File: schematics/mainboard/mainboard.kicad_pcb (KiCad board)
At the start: 2 copper layers, 86.1 x 79.8 mm, 71 parts, among them J1 ICSP, J10 Conn_01x02_Pin, J2 USB_B_Micro, J3 DEALON DC-S050-200, J4 PWR_SELECT, J5 JOY1, J6 JOY2, J7 Conn_01x06_Pin, J8 DGAUGES, J9 LCD, Q2 BC849, U1 ATmega2560-16A, U2 FT232RL, U3 USBLC6-2P6, U4 AIP78M05, U5 L9110, U6 74HC595, U7 74HC595, U8 74HC165, Y1 16Mhz

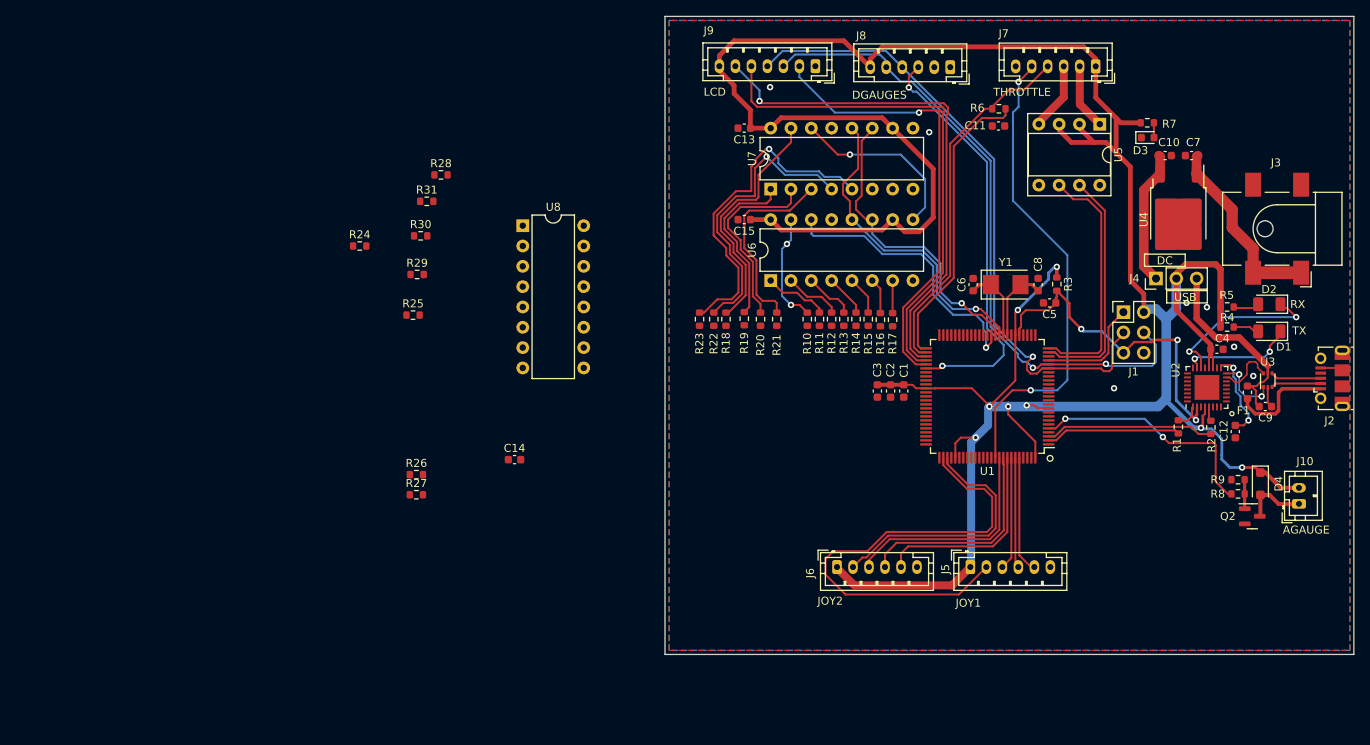
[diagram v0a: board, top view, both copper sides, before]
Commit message: SCH: Mainboard=> LED/Buttons routing(2)
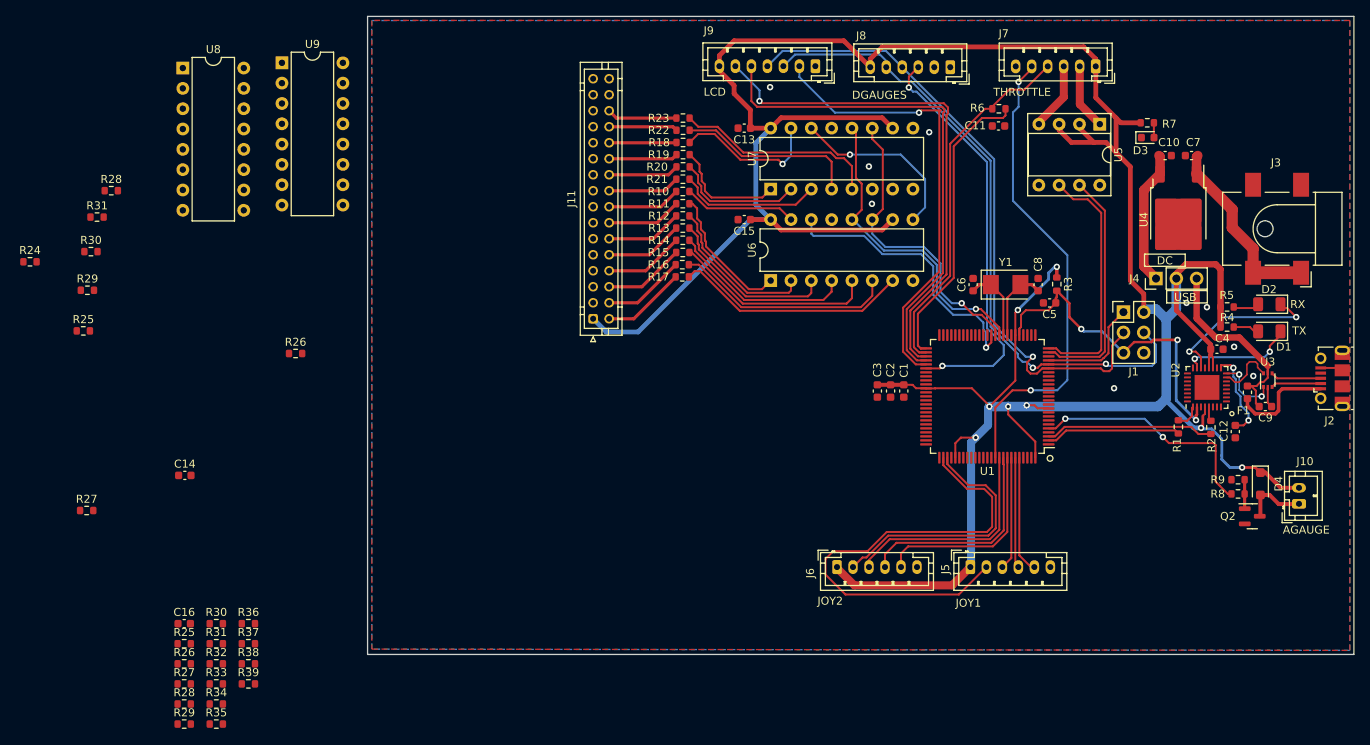
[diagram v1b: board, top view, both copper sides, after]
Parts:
- added C16: 0.1 µf, Capacitor_SMD:C_0603_1608Metric, F.Cu at (58.3, 98.3)
- added J11: Conn_02x16_Counter_Clockwise, Connector_JST:JST_PHD_B32B-PHDSS_2x16_P2.00mm_Vertical, F.Cu at (109.4, 60.1)
- added R25: 10K, Resistor_SMD:R_0603_1608Metric, F.Cu at (58.3, 100.8)
- added R26: 10K, Resistor_SMD:R_0603_1608Metric, F.Cu at (58.3, 103.3)
- added R27: 10K, Resistor_SMD:R_0603_1608Metric, F.Cu at (58.3, 105.8)
- added R28: 10K, Resistor_SMD:R_0603_1608Metric, F.Cu at (58.3, 108.3)
- added R29: 10K, Resistor_SMD:R_0603_1608Metric, F.Cu at (58.3, 110.8)
- added R30: 10K, Resistor_SMD:R_0603_1608Metric, F.Cu at (62.3, 98.3)
- added R31: 10K, Resistor_SMD:R_0603_1608Metric, F.Cu at (62.3, 100.8)
- added R32: 10K, Resistor_SMD:R_0603_1608Metric, F.Cu at (62.3, 103.3)
- added R33: 10K, Resistor_SMD:R_0603_1608Metric, F.Cu at (62.3, 105.8)
- added R34: 10K, Resistor_SMD:R_0603_1608Metric, F.Cu at (62.3, 108.3)
- added R35: 10K, Resistor_SMD:R_0603_1608Metric, F.Cu at (62.3, 110.8)
- added R36: 10K, Resistor_SMD:R_0603_1608Metric, F.Cu at (66.3, 98.3)
- added R37: 10K, Resistor_SMD:R_0603_1608Metric, F.Cu at (66.3, 100.8)
- added R38: 10K, Resistor_SMD:R_0603_1608Metric, F.Cu at (66.3, 103.3)
- added R39: 10K, Resistor_SMD:R_0603_1608Metric, F.Cu at (66.3, 105.8)
- added U9: 74HC165, Package_DIP:DIP-16_W7.62mm, F.Cu at (70.5, 28.2)
- R24: value R? -> 10K
- moved U8 46.8 mm to (58.1, 28.8)
- moved C14 41.3 mm to (58.3, 79.7)
- moved R27 41.3 mm to (46.1, 84.1)
- moved R28 41.3 mm to (49.1, 44.1)
- moved R29 41.3 mm to (46.2, 56.6)
- moved R30 41.3 mm to (46.6, 51.8)
- moved R31 41.3 mm to (47.4, 47.4)
- moved R24 41.3 mm to (39.0, 53.0)
- moved R25 41.3 mm to (45.7, 61.7)
- moved R17 26.8 mm to (120.5, 54.9), turned to 0 degrees
- moved R16 25.7 mm to (120.5, 53.4), turned to 0 degrees
- moved R23 25.2 mm to (120.6, 35.1), turned to 0 degrees
- moved R15 24.6 mm to (120.6, 51.9), turned to 0 degrees
- moved R22 23.9 mm to (120.6, 36.6), turned to 0 degrees
- moved R14 23.8 mm to (120.6, 50.3), turned to 0 degrees
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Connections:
- R10 pad 1: unconnected-(R10-Pad1) -> /QAU6
- R11 pad 1: unconnected-(R11-Pad1) -> /QBU6
- R12 pad 1: unconnected-(R12-Pad1) -> /QCU6
- R13 pad 1: unconnected-(R13-Pad1) -> /QDU6
- R14 pad 1: unconnected-(R14-Pad1) -> /QEU6
- R15 pad 1: unconnected-(R15-Pad1) -> /QFU6
- R16 pad 1: unconnected-(R16-Pad1) -> /QGU6
- R17 pad 1: unconnected-(R17-Pad1) -> /QHU6
- R18 pad 1: unconnected-(R18-Pad1) -> /QAU7
- R19 pad 1: unconnected-(R19-Pad1) -> /QBU7
- R20 pad 1: unconnected-(R20-Pad1) -> /QCU7
- R21 pad 1: unconnected-(R21-Pad1) -> /QDU7
- R22 pad 1: unconnected-(R22-Pad1) -> /QEU7
- R23 pad 1: unconnected-(R23-Pad1) -> /QFU7
- R24 pad 2: unconnected-(R24-Pad2) -> GND
- U7 pad 6: unconnected-(U7-QG-Pad6) -> GND
- U7 pad 7: unconnected-(U7-QH-Pad7) -> GND
- U7 pad 9: unconnected-(U7-QH'-Pad9) -> GND
- U8 pad 1: unconnected-(U8-~{PL}-Pad1) -> /LATCH
- U8 pad 15: unconnected-(U8-~{CE}-Pad15) -> GND
- U8 pad 2: unconnected-(U8-CP-Pad2) -> /SCK
- U8 pad 7: unconnected-(U8-~{Q7}-Pad7) -> GND
- U8 pad 9: unconnected-(U8-Q7-Pad9) -> Net-(U8-Q7)
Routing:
- net Net-(U6-QH): track 4.06 -> 29.4 mm
- net Net-(U6-QG): track 4.48 -> 27.6 mm
- net +5V: track 357.7 -> 379.6 mm
- net Net-(U6-QF): track 4.84 -> 25.5 mm
- net Net-(U6-QE): track 5.26 -> 23.0 mm
- net Net-(U7-QF): track 42.1 -> 25.7 mm, vias 1 -> 0
- net Net-(U6-QD): track 6.28 -> 21.4 mm
- net Net-(U7-QE): track 36.7 -> 22.8 mm, vias 1 -> 0
- net Net-(U6-QC): track 7.15 -> 19.4 mm
- net Net-(U7-QA): track 30.5 -> 18.5 mm, vias 0 -> 1
- net /QHU6: track 0.00 -> 10.5 mm
- net /QGU6: track 0.00 -> 10.3 mm
- net /QFU6: track 0.00 -> 10.2 mm
- net /QEU6: track 0.00 -> 9.96 mm
- net /QDU6: track 0.00 -> 9.76 mm
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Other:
- board size 86.1 x 79.8 mm -> 123.3 x 79.8 mm

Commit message: SCH: MAinboard=> Clean DRC issues
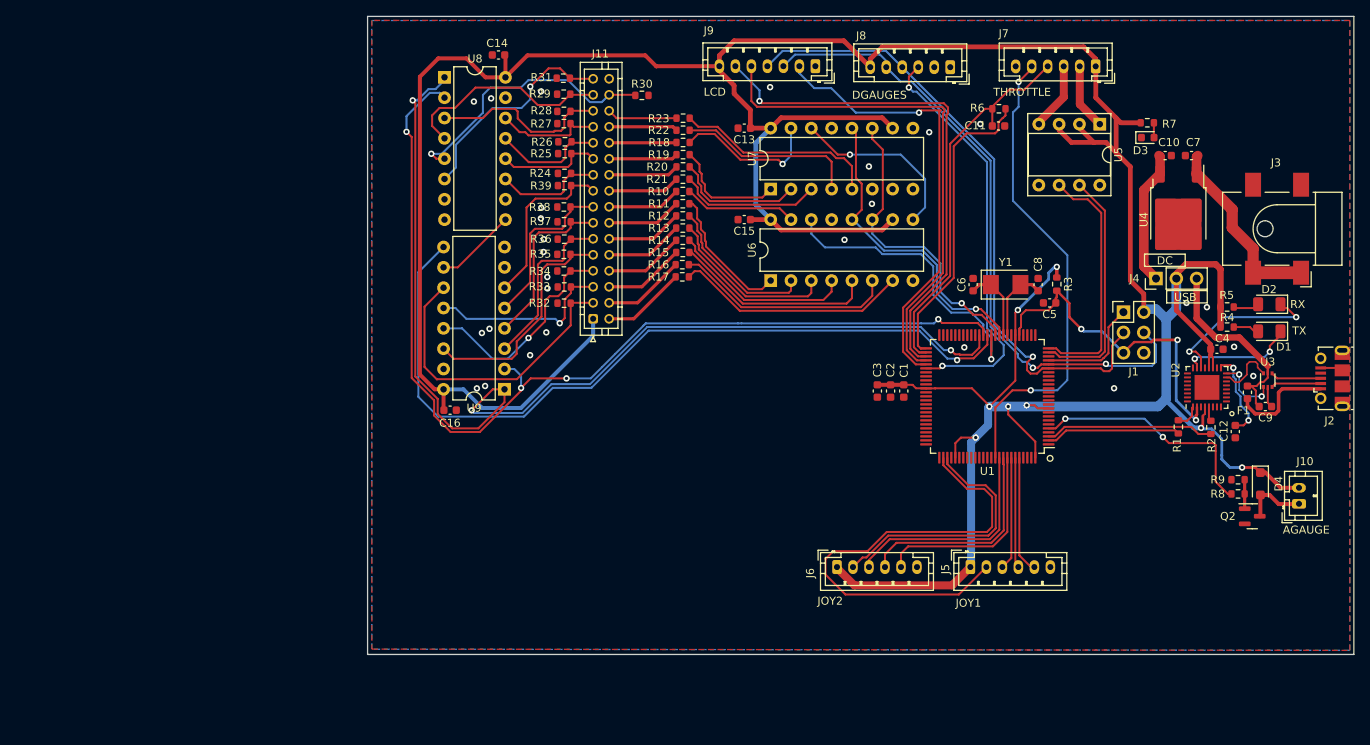
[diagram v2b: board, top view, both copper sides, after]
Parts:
- removed the R25 at (58.3, 100.8)
- removed the R25 at (45.7, 61.7)
- removed the R26 at (72.2, 64.5)
- removed the R26 at (58.3, 103.3)
- removed the R27 at (58.3, 105.8)
- removed the R27 at (46.1, 84.1)
- removed the R28 at (49.1, 44.1)
- removed the R28 at (58.3, 108.3)
- removed the R29 at (58.3, 110.8)
- removed the R29 at (46.2, 56.6)
- removed the R30 at (62.3, 98.3)
- removed the R30 at (46.6, 51.8)
- removed the R31 at (47.4, 47.4)
- removed the R31 at (62.3, 100.8)
- added R25: 10K, Resistor_SMD:R_0603_1608Metric, F.Cu at (105.8, 39.5)
- added R26: 10K, Resistor_SMD:R_0603_1608Metric, F.Cu at (105.8, 38.0)
- added R27: 10K, Resistor_SMD:R_0603_1608Metric, F.Cu at (105.7, 35.8)
- added R28: 10K, Resistor_SMD:R_0603_1608Metric, F.Cu at (105.7, 34.2)
- added R29: 10K, Resistor_SMD:R_0603_1608Metric, F.Cu at (105.7, 32.1)
- added R30: 10K, Resistor_SMD:R_0603_1608Metric, F.Cu at (115.5, 32.2)
- added R31: 10K, Resistor_SMD:R_0603_1608Metric, F.Cu at (105.7, 30.1)
- moved R39 73.8 mm to (105.8, 43.5), turned to 180 degrees
- moved R35 73.0 mm to (105.7, 52.1), turned to 180 degrees
- moved R34 69.4 mm to (105.7, 54.2), turned to 180 degrees
- moved R38 69.4 mm to (105.7, 46.2), turned to 180 degrees
- moved R24 67.7 mm to (105.8, 42.0), turned to 180 degrees
- moved R33 66.0 mm to (105.8, 56.2), turned to 180 degrees
- moved R37 65.9 mm to (105.8, 48.0), turned to 180 degrees
- moved C14 65.6 mm to (97.5, 27.2), turned to 180 degrees
- moved R32 62.6 mm to (105.8, 58.2), turned to 180 degrees
- moved R36 62.2 mm to (105.8, 50.2), turned to 180 degrees
- moved U9 49.4 mm to (98.3, 69.0), turned to 180 degrees
- moved C16 42.6 mm to (91.5, 71.6)
- moved U8 32.7 mm to (90.8, 30.0)
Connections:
- net /QAU6 renamed /U6Q0
- net /QAU7 renamed /U7Q0
- net /QBU6 renamed /U6Q1
- net /QBU7 renamed /U7Q1
- net /QCU6 renamed /U6Q2
- net /QCU7 renamed /U7Q2
- net /QDU6 renamed /U6Q3
- net /QDU7 renamed /U7Q3
- net /QEU6 renamed /U6Q4
- net /QEU7 renamed /U7Q4
- net /QFU6 renamed /U6Q5
- net /QGU6 renamed /U6Q6
- net /QHU6 renamed /U6Q7
- J11 pad 11: unconnected-(J11-Pin_11-Pad11) -> /U9D4
- J11 pad 13: unconnected-(J11-Pin_13-Pad13) -> /U9D5
- J11 pad 15: unconnected-(J11-Pin_15-Pad15) -> /U9D6
- J11 pad 17: unconnected-(J11-Pin_17-Pad17) -> /U9D7
- J11 pad 19: unconnected-(J11-Pin_19-Pad19) -> /U8D0
- J11 pad 21: unconnected-(J11-Pin_21-Pad21) -> /U8D1
- J11 pad 23: unconnected-(J11-Pin_23-Pad23) -> /U8D2
- J11 pad 25: unconnected-(J11-Pin_25-Pad25) -> /U8D3
- J11 pad 27: unconnected-(J11-Pin_27-Pad27) -> /U8D4
- J11 pad 28: unconnected-(J11-Pin_28-Pad28) -> /U7Q5
- J11 pad 29: unconnected-(J11-Pin_29-Pad29) -> /U8D5
- J11 pad 3: unconnected-(J11-Pin_3-Pad3) -> /U9D0
- J11 pad 30: unconnected-(J11-Pin_30-Pad30) -> /U8D6
- J11 pad 31: unconnected-(J11-Pin_31-Pad31) -> /U8D7
- J11 pad 5: unconnected-(J11-Pin_5-Pad5) -> /U9D1
- J11 pad 7: unconnected-(J11-Pin_7-Pad7) -> /U9D2
- J11 pad 9: unconnected-(J11-Pin_9-Pad9) -> /U9D3
- R23 pad 1: /QFU7 -> /U7Q5
- R24 pad 1: Net-(U8-D7) -> /U8D0
- R32 pad 1: Net-(U9-D0) -> /U9D0
- R33 pad 1: Net-(U9-D1) -> /U9D1
- R34 pad 1: Net-(U9-D2) -> /U9D2
- R35 pad 1: Net-(U9-D3) -> /U9D3
- R36 pad 1: Net-(U9-D4) -> /U9D4
- R37 pad 1: Net-(U9-D5) -> /U9D5
- R38 pad 1: Net-(U9-D6) -> /U9D6
- R39 pad 1: Net-(U9-D7) -> /U9D7
- U1 pad 38: unconnected-(U1-PL3-Pad38) -> /SAS_SEROUT
- U1 pad 39: unconnected-(U1-PL4-Pad39) -> /SAS_SCK
- U1 pad 40: unconnected-(U1-PL5-Pad40) -> /SAS_LATCH
- U7 pad 6: GND -> unconnected-(U7-QG-Pad6)
- U7 pad 7: GND -> unconnected-(U7-QH-Pad7)
- U7 pad 9: GND -> unconnected-(U7-QH'-Pad9)
- U8 pad 1: /LATCH -> /SAS_LATCH
- U8 pad 11: Net-(U8-D0) -> /U8D0
- U8 pad 12: Net-(U8-D1) -> /U8D1
- U8 pad 13: Net-(U8-D2) -> /U8D2
- U8 pad 14: Net-(U8-D3) -> /U8D3
- U8 pad 2: /SCK -> /SAS_SCK
- U8 pad 3: Net-(U8-D4) -> /U8D4
- U8 pad 4: Net-(U8-D5) -> /U8D5
- U8 pad 5: Net-(U8-D6) -> /U8D6
- U8 pad 6: Net-(U8-D7) -> /U8D7
- U8 pad 7: GND -> unconnected-(U8-~{Q7}-Pad7)
- U9 pad 1: /LATCH -> /SAS_LATCH
- U9 pad 11: Net-(U9-D0) -> /U9D0
- U9 pad 12: Net-(U9-D1) -> /U9D1
- U9 pad 13: Net-(U9-D2) -> /U9D2
- U9 pad 14: Net-(U9-D3) -> /U9D3
- U9 pad 2: /SCK -> /SAS_SCK
- U9 pad 3: Net-(U9-D4) -> /U9D4
- U9 pad 4: Net-(U9-D5) -> /U9D5
- U9 pad 5: Net-(U9-D6) -> /U9D6
- U9 pad 6: Net-(U9-D7) -> /U9D7
- U9 pad 7: GND -> unconnected-(U9-~{Q7}-Pad7)
- U9 pad 9: /SEROUT -> /SAS_SEROUT
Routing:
- net /SAS_LATCH: track 0.00 -> 134.5 mm, vias 0 -> 3
- net /SAS_SCK: track 0.00 -> 125.9 mm, vias 0 -> 4
- net /SAS_SEROUT: track 0.00 -> 100.2 mm, vias 0 -> 1
- net +5V: track 379.6 -> 463.9 mm
- net /U9D0: track 0.00 -> 38.2 mm
- net /U8D6: track 0.00 -> 34.1 mm, vias 0 -> 1
- net /U9D3: track 0.00 -> 29.3 mm
- net /U8D7: track 0.00 -> 27.4 mm, vias 0 -> 1
- net /U9D2: track 0.00 -> 27.3 mm, vias 0 -> 1
- net /U8D5: track 0.00 -> 26.6 mm
- net /U9D1: track 0.00 -> 23.2 mm, vias 0 -> 1
- net /U8D4: track 0.00 -> 22.5 mm
- net /U9D5: track 0.00 -> 21.6 mm
- net /U9D7: track 0.00 -> 21.5 mm
- net /U9D4: track 0.00 -> 21.4 mm
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
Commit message: SCH:MB=> fixes + gen jlc fab prj
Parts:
- C1, C2, C3, C5: value 0.1uF -> 100nF
- C13, C14, C15, C16: value 0.1 µf -> 100nF
- J10: value Conn_01x02_Pin -> Conn_AGauge
- J11: value Conn_02x16_Counter_Clockwise -> Conn_SAS
- J5: value JOY1 -> Conn_Joy1
- J6: value JOY2 -> Conn_Joy2
- J7: value Conn_01x06_Pin -> Conn_Throttle
- J8: value DGAUGES -> Conn_DGauges
- J9: value LCD -> Conn_LCD
- moved C9 5.96 mm to (196.4, 66.0)
- moved J1 0.71 mm to (176.1, 59.9)
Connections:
- C9 pad 1: Net-(J4-Pin_3) -> +5V
- C9 pad 2: Net-(U3-GND) -> GND
- U3 pad 2: Net-(U3-GND) -> GND
- U3 pad 5: Net-(J4-Pin_3) -> +5V
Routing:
- net +5V: track 463.9 -> 473.8 mm
- net Net-(J4-Pin_3): track 23.8 -> 30.2 mm, vias 0 -> 1
- net /RESET: track 41.9 -> 36.7 mm
- net Net-(U3-GND): track 2.57 -> 0.00 mm
- net /SCK: track 80.2 -> 80.8 mm
- net GND: track 2.82 -> 3.44 mm

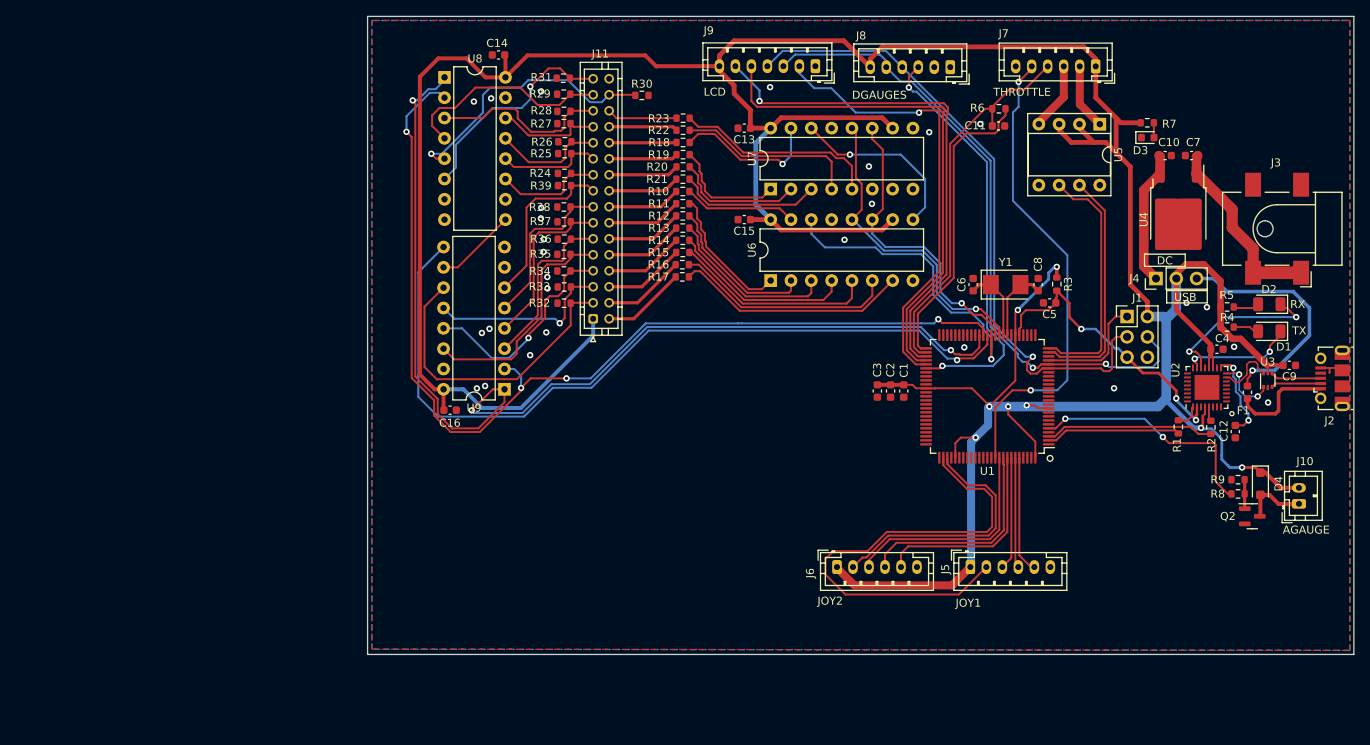
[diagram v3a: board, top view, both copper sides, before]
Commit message: SCH:MB=> Changed FT232 package
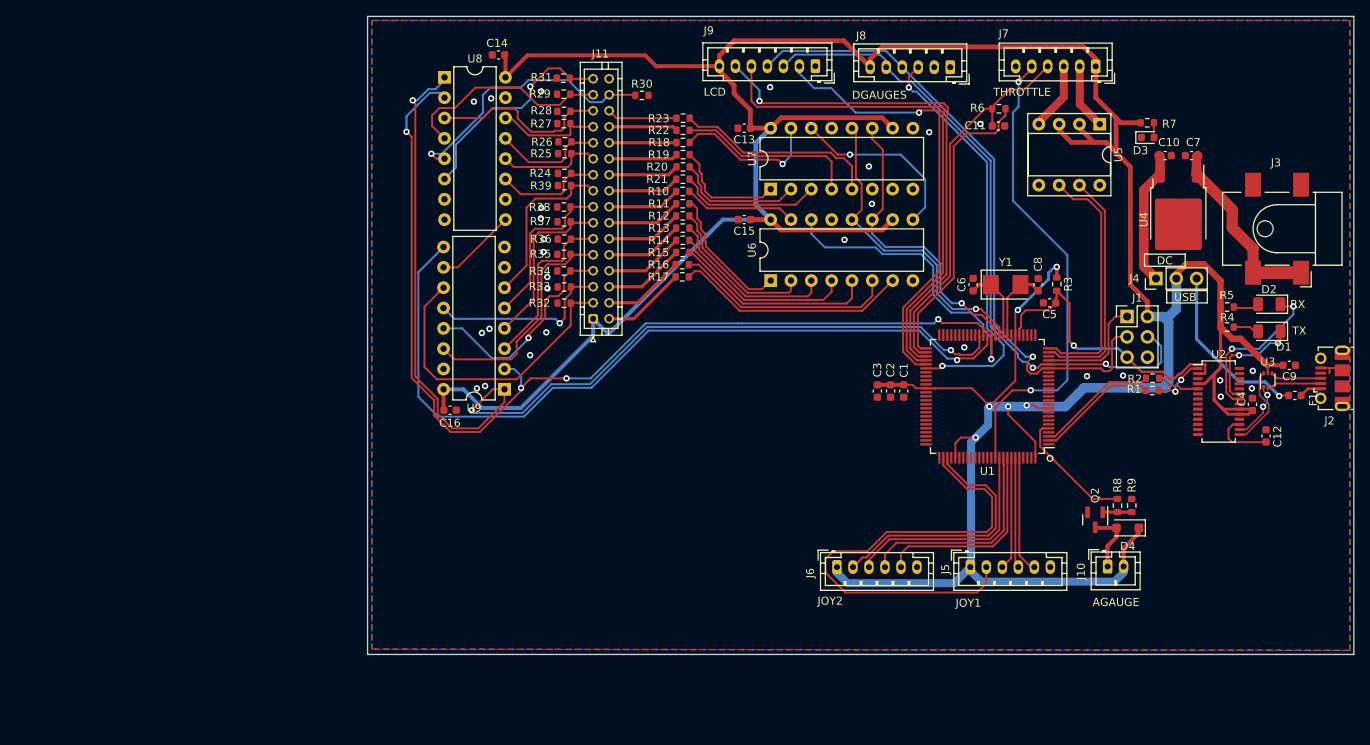
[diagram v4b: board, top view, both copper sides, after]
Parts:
- U2: footprint Package_DFN_QFN:HVQFN-32-1EP_5x5mm_P0.5mm_EP3.1x3.1mm -> Package_SO:SSOP-28_3.9x9.9mm_P0.635mm
- moved J10 25.2 mm to (173.7, 91.1), turned to 0 degrees
- moved Q2 19.6 mm to (172.1, 85.3), turned to -90 degrees
- moved D4 17.5 mm to (176.2, 86.3), turned to 180 degrees
- moved R8 15.1 mm to (174.9, 83.5), turned to -90 degrees
- moved R9 13.7 mm to (176.7, 83.5), turned to -90 degrees
- moved R2 9.53 mm to (179.3, 67.6), turned to 180 degrees
- moved C4 8.20 mm to (191.8, 70.8), turned to 90 degrees
- moved F1 5.95 mm to (197.1, 69.7), turned to 180 degrees
- moved R1 5.60 mm to (179.3, 69.1), turned to 180 degrees
- moved C12 3.88 mm to (193.5, 74.8), turned to 90 degrees
- moved U2 2.29 mm to (187.6, 70.5), turned to 0 degrees
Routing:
- net +5V: track 473.8 -> 457.7 mm, vias 8 -> 6
- net Net-(U1-PE3): track 29.9 -> 15.6 mm, vias 2 -> 0
- net Net-(J2-VBUS): track 13.1 -> 2.79 mm
- net Net-(J4-Pin_3): track 30.2 -> 22.0 mm
- net /FTDI_RX: track 21.1 -> 15.2 mm
- net Net-(U2-RXD): track 1.49 -> 5.38 mm
- net Net-(U2-3V3OUT): track 11.3 -> 7.70 mm, vias 2 -> 0
- net Net-(U2-TXD): track 3.24 -> 6.66 mm, vias 0 -> 2
- net /D+: track 7.52 -> 10.3 mm
- net /FTDI_TX: track 16.9 -> 15.2 mm
- net /RESET: track 36.7 -> 37.8 mm, vias 3 -> 1
- net /MOSI: track 80.9 -> 81.7 mm
- net /JOY1_PB: track 59.4 -> 60.3 mm
- net Net-(D2-K): track 20.7 -> 19.9 mm
- net GND: vias 27 -> 28
